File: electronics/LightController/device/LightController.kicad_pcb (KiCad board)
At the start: 2 copper layers, 16 parts, among them J1 RF_TX, J2 AC, J3 SERIAL, J4 ICSP, SW1 RotaryEncoder_Switch, U1 ATMEGA328P-AU, U2 5V07 Transformer, Y1 16MHz

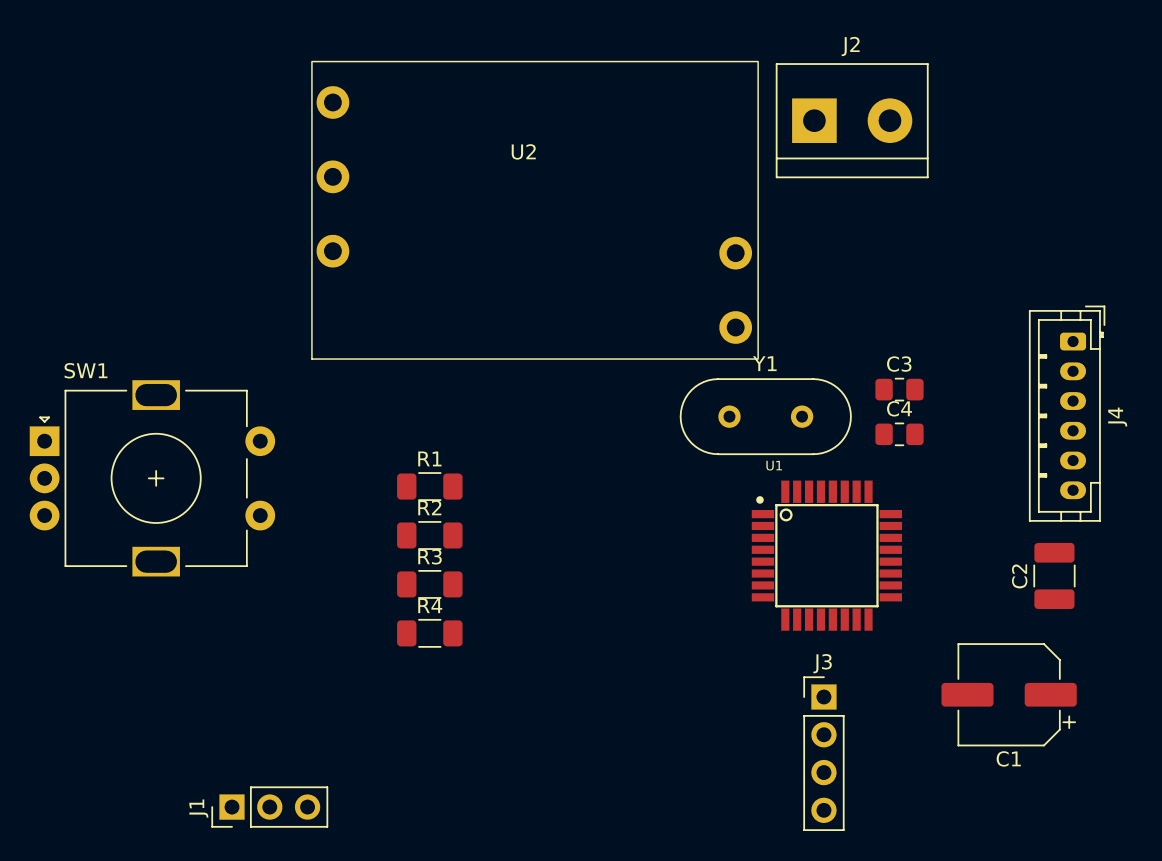
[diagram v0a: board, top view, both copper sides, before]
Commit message: Arrance components in LightController PCB
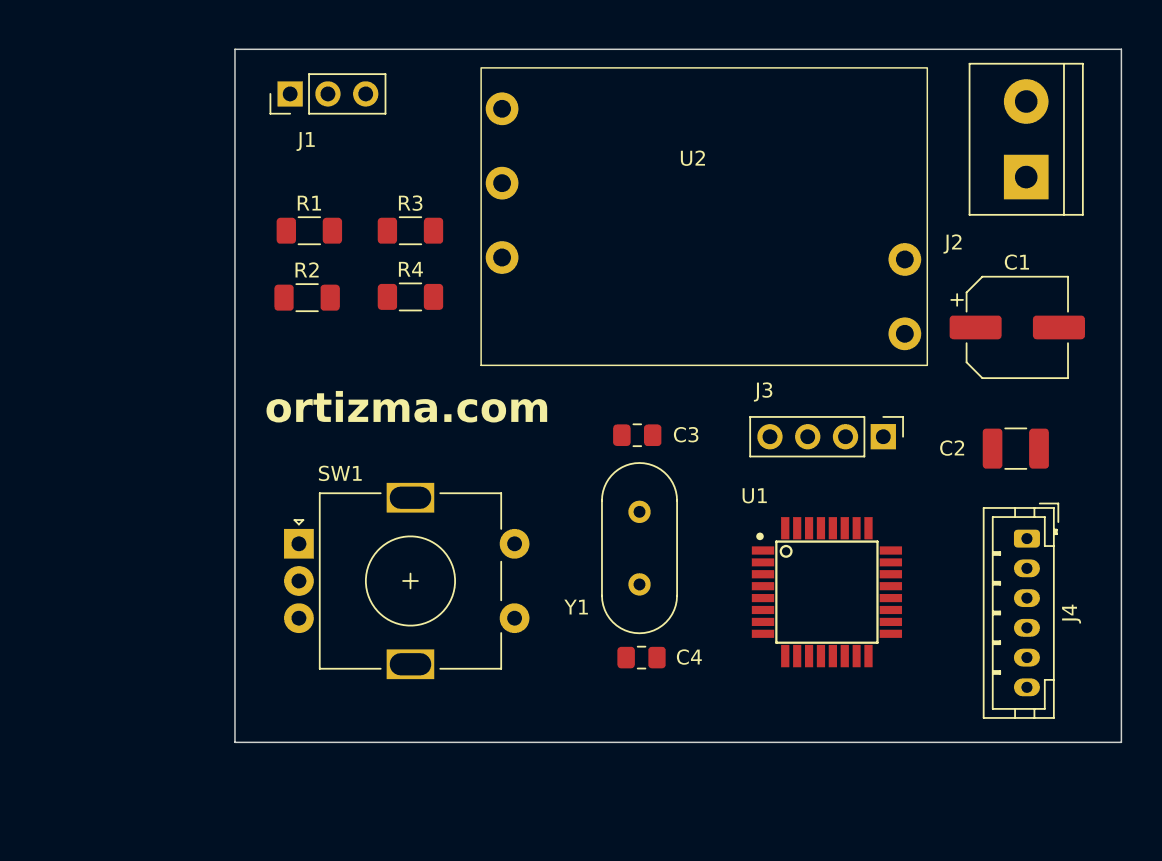
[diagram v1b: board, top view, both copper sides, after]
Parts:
- moved J1 48.1 mm to (88.0, 41.1)
- moved C1 24.7 mm to (136.9, 56.9), turned to 0 degrees
- moved R3 23.8 mm to (96.1, 50.4)
- moved C4 22.9 mm to (111.6, 79.0), turned to 180 degrees
- moved R4 22.7 mm to (96.1, 54.8)
- moved R1 19.0 mm to (89.3, 50.4)
- moved SW1 18.4 mm to (88.6, 71.4)
- moved R2 18.0 mm to (89.2, 54.9)
- moved J3 17.9 mm to (127.9, 64.2), turned to -90 degrees
- moved C3 17.9 mm to (111.3, 64.1), turned to 180 degrees
- moved J2 14.7 mm to (137.5, 46.7), turned to 90 degrees
- moved J4 13.6 mm to (137.6, 71.0)
- moved Y1 12.8 mm to (111.5, 74.1), turned to 90 degrees
- moved U2 11.4 mm to (115.4, 49.6)
- moved C2 8.95 mm to (136.8, 65.0), turned to 0 degrees
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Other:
- board outline added: 59.6 x 46.6 mm
- board text added: "ortizma.com"

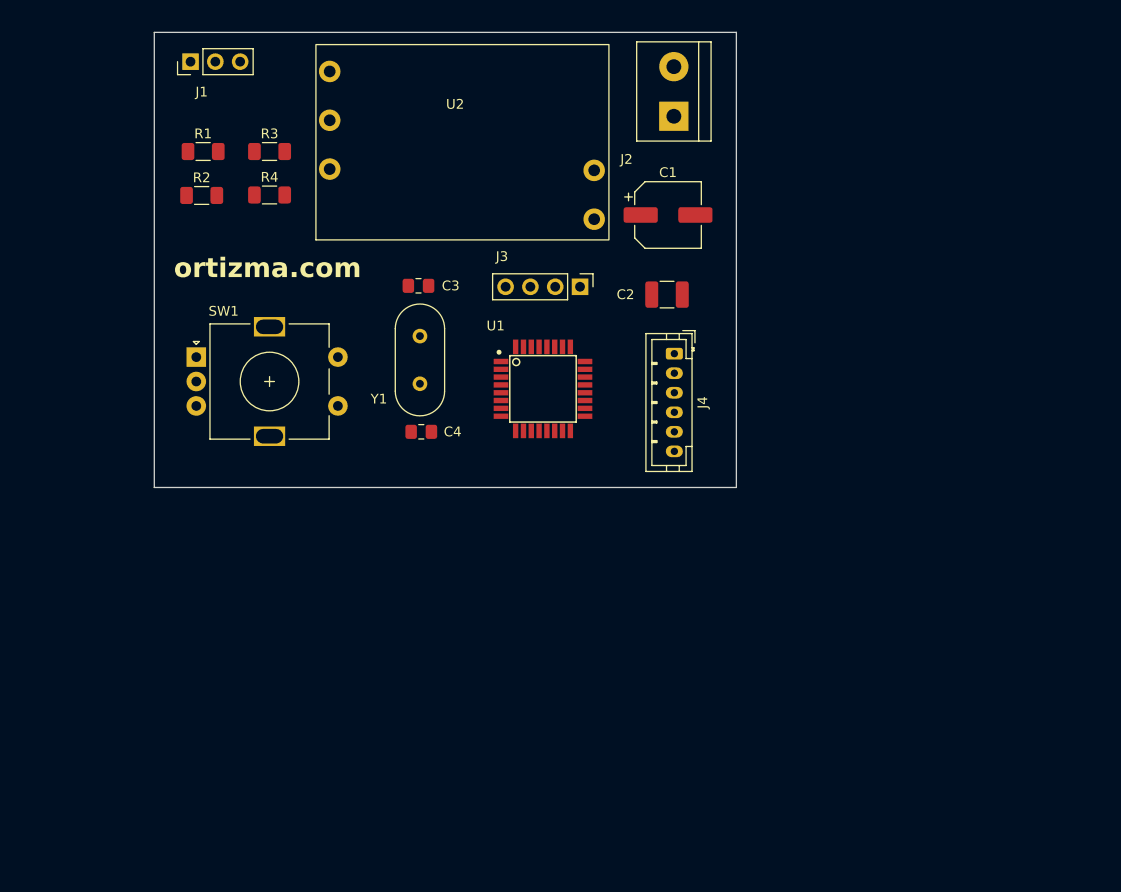
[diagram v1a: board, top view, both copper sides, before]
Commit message: Finish LightController PCB design with 3 switches
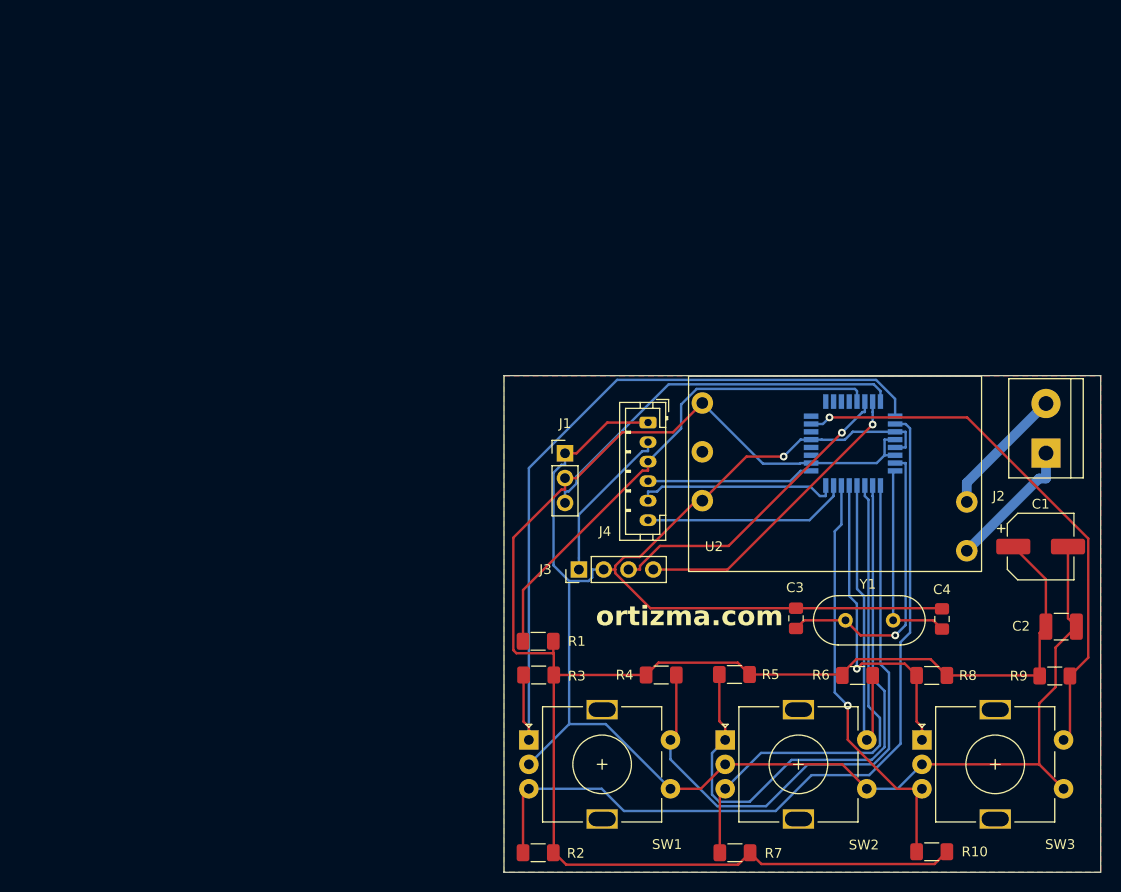
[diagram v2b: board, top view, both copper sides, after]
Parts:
- added R10: 10K, Resistor_SMD:R_1206_3216Metric_Pad1.30x1.75mm_HandSolder, F.Cu at (163.9, 122.0)
- added R5: 10K, Resistor_SMD:R_1206_3216Metric_Pad1.30x1.75mm_HandSolder, F.Cu at (143.7, 103.9)
- added R6: 10K, Resistor_SMD:R_1206_3216Metric_Pad1.30x1.75mm_HandSolder, F.Cu at (156.3, 104.0)
- added R7: 10K, Resistor_SMD:R_1206_3216Metric_Pad1.30x1.75mm_HandSolder, F.Cu at (143.8, 122.2)
- added R8: 10K, Resistor_SMD:R_1206_3216Metric_Pad1.30x1.75mm_HandSolder, F.Cu at (163.9, 104.0)
- added R9: 10K, Resistor_SMD:R_1206_3216Metric_Pad1.30x1.75mm_HandSolder, F.Cu at (176.5, 104.0)
- added SW2: RotaryEncoder_Switch, AA_Footprints:RotaryEncoder_Alps_EC11E-Switch_Vertical_H20mm, F.Cu at (142.8, 110.6)
- added SW3: RotaryEncoder_Switch, AA_Footprints:RotaryEncoder_Alps_EC11E-Switch_Vertical_H20mm, F.Cu at (162.9, 110.6)
- U1: moved to B.Cu
- moved R2 75.6 mm to (123.6, 122.2)
- moved R4 63.4 mm to (136.2, 104.0)
- moved R1 60.8 mm to (123.6, 100.5)
- moved R3 60.3 mm to (123.7, 104.0)
- moved C4 56.7 mm to (165.0, 98.2), turned to -90 degrees
- moved J1 55.5 mm to (126.4, 81.2), turned to 0 degrees
- moved Y1 54.2 mm to (160.0, 98.3), turned to 180 degrees
- moved C2 52.8 mm to (177.2, 99.0)
- moved SW1 51.9 mm to (122.7, 110.6)
- moved C3 51.5 mm to (150.0, 98.2), turned to -90 degrees
- moved J2 51.4 mm to (175.6, 81.2)
- moved U2 51.1 mm to (153.6, 83.5)
- moved C1 51.1 mm to (175.1, 90.8)
- moved U1 32.2 mm to (155.9, 80.2), turned to 180 degrees
- moved J3 29.0 mm to (127.8, 93.2), turned to 90 degrees
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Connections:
- U1 pad 10: unconnected-(U1-PD6-Pad10) -> /PD6
- U1 pad 11: unconnected-(U1-PD7-Pad11) -> /PD7
- U1 pad 12: unconnected-(U1-PB0-Pad12) -> /PB0
- U1 pad 13: unconnected-(U1-PB1-Pad13) -> /PB1
- U1 pad 14: unconnected-(U1-PB2-Pad14) -> /PB2
- U1 pad 23: unconnected-(U1-PC0-Pad23) -> /PC0
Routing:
- net GND: track 0.00 -> 206.0 mm, vias 0 -> 1
- net +5V: track 0.00 -> 198.0 mm
- net /PD4: track 0.00 -> 83.1 mm
- net /PD3: track 0.00 -> 78.5 mm
- net /PD5: track 0.00 -> 63.0 mm
- net /PD6: track 0.00 -> 60.7 mm
- net /PC0: track 0.00 -> 55.5 mm, vias 0 -> 1
- net /PD7: track 0.00 -> 51.7 mm
- net /RESET: track 0.00 -> 51.1 mm
- net /PB2: track 0.00 -> 43.0 mm, vias 0 -> 1
- net /PD2: track 0.00 -> 39.8 mm
- net /PB0: track 0.00 -> 33.3 mm
- net /PB1: track 0.00 -> 32.7 mm, vias 0 -> 1
- net /TX: track 0.00 -> 32.2 mm, vias 0 -> 1
- net /RX: track 0.00 -> 31.0 mm, vias 0 -> 1
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- added copper zone on F.Cu, net GND
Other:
- board size 59.6 x 46.6 mm -> 61.1 x 50.9 mm

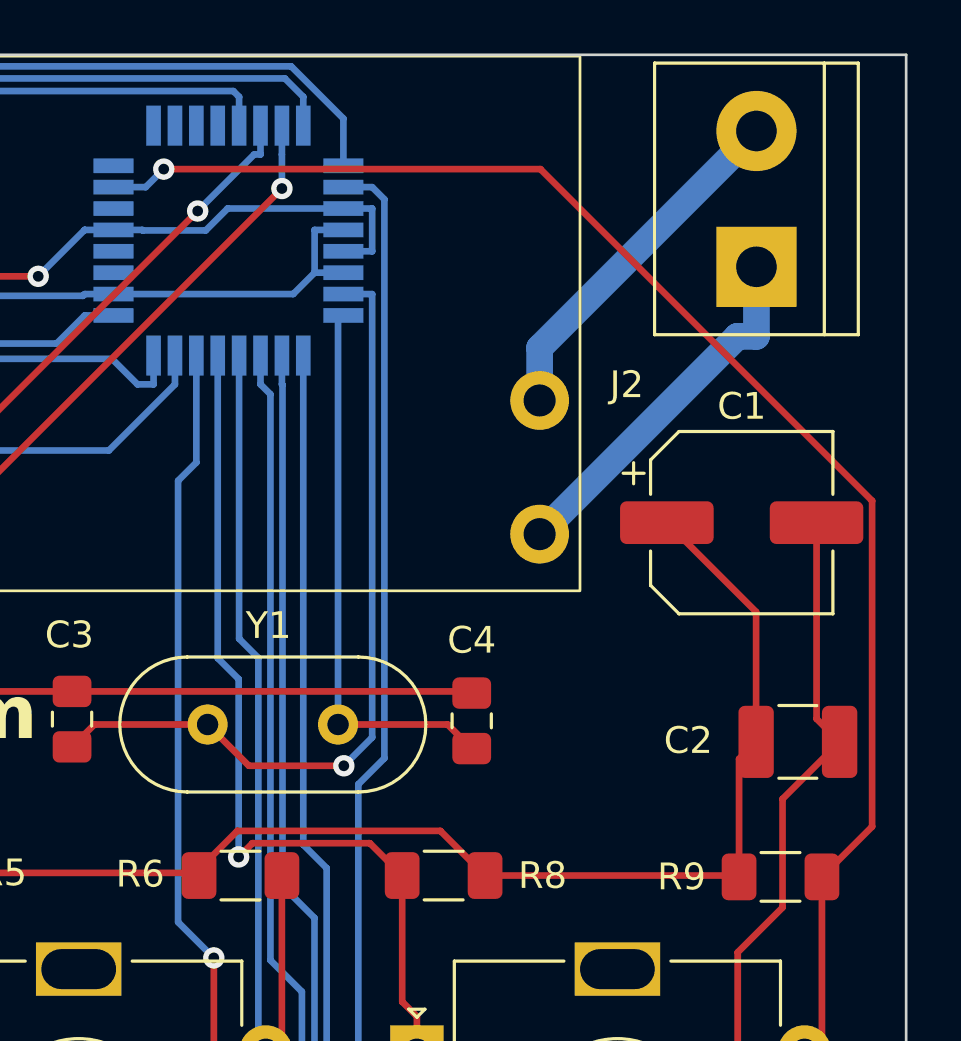
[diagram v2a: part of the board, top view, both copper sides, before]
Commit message: Improved the designs of LightController & LightDimmer PCBs
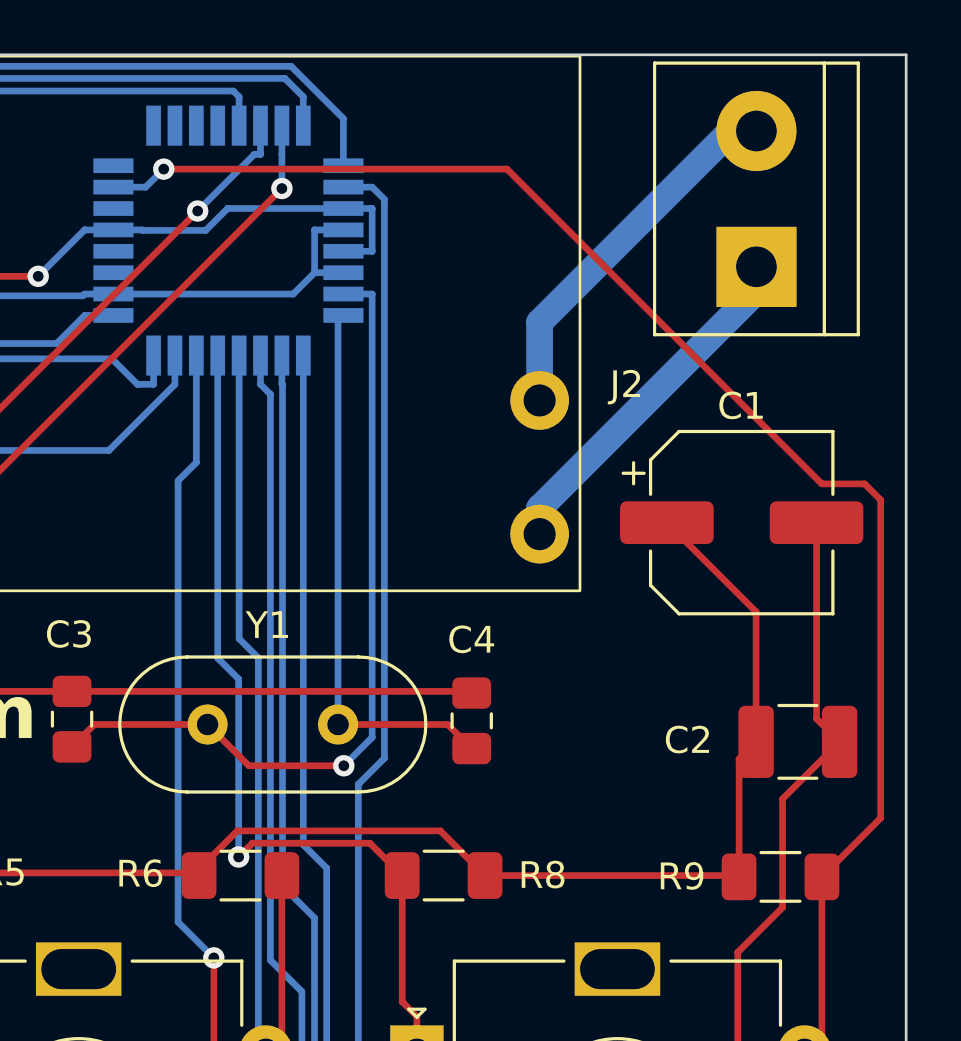
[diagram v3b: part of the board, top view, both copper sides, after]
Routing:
- net Net-(J2-AC_N): track 13.4 -> 14.0 mm

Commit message: Small adjustments before JLC order
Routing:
- added copper zone on B.Cu, net GND
